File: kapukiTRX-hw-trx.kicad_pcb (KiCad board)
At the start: 4 copper layers, 45.7 x 27.9 mm, 73 parts, among them J1 GPS, J10 Conn_01x01, J11 Conn_01x01, J12 Conn_01x01, J13 Conn_01x01, J14 Conn_01x01, J15 Conn_01x01, J16 Conn_01x01, J17 Conn_01x01, J18 Conn_01x01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

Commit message: Use crystal with smaller footprint
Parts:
- added C33: 100n, Capacitor_SMD:C_0402_1005Metric, F.Cu at (226.1, 99.1)
- added C34: 100n, Capacitor_SMD:C_0402_1005Metric, F.Cu at (223.5, 104.6)
- added C35: 6n8, Capacitor_SMD:C_0402_1005Metric, F.Cu at (229.0, 99.1)
- added C36: 120n, Capacitor_SMD:C_0402_1005Metric, F.Cu at (226.1, 101.0)
- added C37: 100n, Capacitor_SMD:C_0402_1005Metric, F.Cu at (229.0, 101.0)
- added C38: 100n, Capacitor_SMD:C_0402_1005Metric, F.Cu at (226.4, 103.0)
- added C39: 22p, Capacitor_SMD:C_0402_1005Metric, F.Cu at (231.9, 99.1)
- added C40: 22p, Capacitor_SMD:C_0402_1005Metric, F.Cu at (226.4, 105.0)
- added R10: 4k7, Resistor_SMD:R_0402_1005Metric, F.Cu at (231.9, 101.0)
- added R11: 4k7, Resistor_SMD:R_0402_1005Metric, F.Cu at (229.3, 103.0)
- added R12: 10k, Resistor_SMD:R_0402_1005Metric, F.Cu at (229.3, 105.0)
- added R13: 10k, Resistor_SMD:R_0402_1005Metric, F.Cu at (232.2, 103.0)
- added U7: BNO055, Package_LGA:LGA-28_5.2x3.8mm_P0.5mm, F.Cu at (221.1, 100.8)
- added Y2: 32.768kHz, Crystal:Crystal_SMD_2012-2Pin_2.0x1.2mm_HandSoldering, F.Cu at (219.8, 105.0)

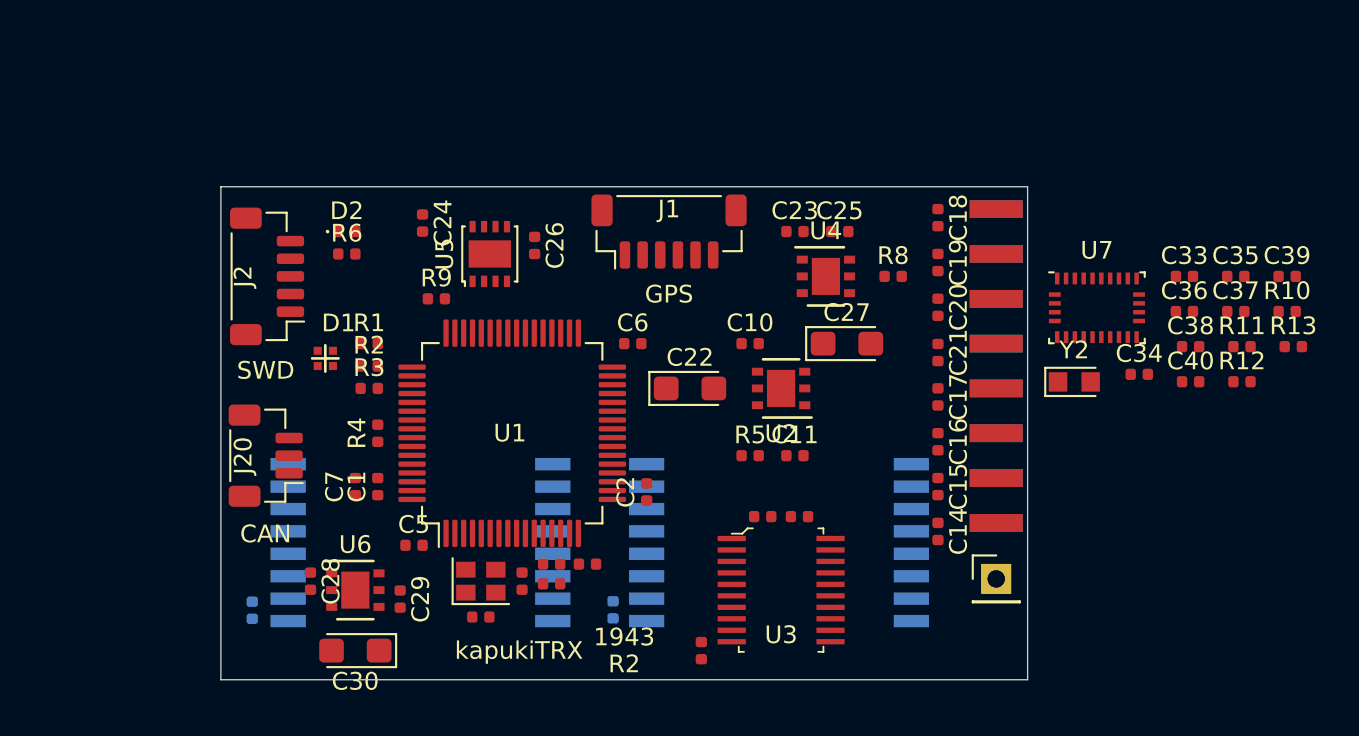
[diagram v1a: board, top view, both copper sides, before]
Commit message: Change processor to G4 series
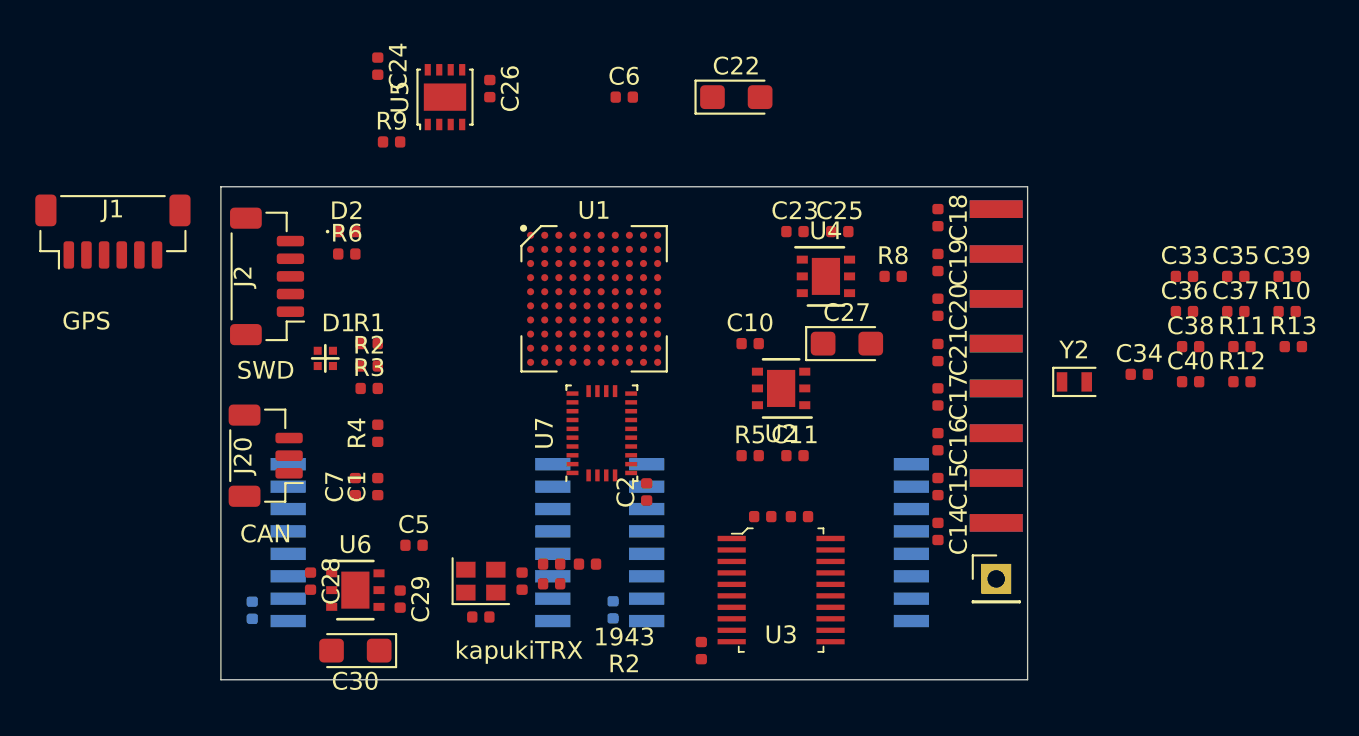
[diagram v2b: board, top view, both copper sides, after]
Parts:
- U1: value STM32L476RGTx -> STM32G474VE; footprint Package_QFP:LQFP-64_10x10mm_P0.5mm -> miscellaneous:TFBGA-100_10x10_8.0x8.0mm
- Y2: footprint Crystal:Crystal_SMD_2012-2Pin_2.0x1.2mm_HandSoldering -> Crystal:Crystal_SMD_2012-2Pin_2.0x1.2mm
- moved J1 31.5 mm to (165.3, 96.5)
- moved U7 28.9 mm to (193.0, 108.0), turned to 90 degrees
- moved C22 16.7 mm to (200.7, 88.9)
- moved C6 14.0 mm to (194.3, 88.9)
- moved C24 9.25 mm to (180.3, 87.1)
- moved C26 9.25 mm to (186.7, 88.4)
- moved R9 9.25 mm to (181.1, 91.4)
- moved U5 9.25 mm to (184.2, 88.9)
- moved U1 8.92 mm to (192.6, 100.3), turned to 0 degrees
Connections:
- R4 pad 2: GND -> Net-(R4-Pad2)
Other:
- net class Default: clearance 0.2 -> 0.127; trace_width 0.25 -> 0.127; via_dia 0.8 -> 0.508; via_drill 0.4 -> 0.254
- rule trace_clearance: 0.2 -> 0.127
- rule trace_min: 0.2 -> 0.127
- rule via_min_drill: 0.3 -> 0.254
- rule via_min_size: 0.4 -> 0.508

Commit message: Placing components and start routing
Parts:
- C1, C2, C35, C36, C6, C7, J10, J12, J14, J16, J18, J4, J6, J8: moved to B.Cu
- J11, J13, J15, J17, J3, J5, J7, J9: moved to F.Cu
- moved J1 43.3 mm to (202.2, 119.3), turned to 180 degrees
- moved C39 42.7 mm to (189.9, 107.1)
- moved R10 41.6 mm to (190.6, 106.2)
- moved R11 38.7 mm to (190.7, 105.0)
- moved C40 37.2 mm to (189.5, 109.2), turned to 270 degrees
- moved C35 36.5 mm to (193.8, 108.7), turned to 270 degrees
- moved R13 35.2 mm to (197.4, 107.6), turned to 270 degrees
- moved R12 34.7 mm to (195.2, 111.6)
- moved C36 32.2 mm to (194.8, 108.7), turned to 270 degrees
- moved C34 31.1 mm to (193.2, 111.6), turned to 180 degrees
- moved R8 29.6 mm to (180.5, 104.8), turned to 90 degrees
- moved Y2 29.1 mm to (191.0, 109.0), turned to 270 degrees
- moved C23 24.3 mm to (180.5, 102.5), turned to 180 degrees
- moved C25 23.9 mm to (185.0, 106.9)
- moved R4 23.7 mm to (196.5, 90.6)
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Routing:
- net IN: track 0.00 -> 106.8 mm, vias 0 -> 5
- net /VCCCPU: track 0.00 -> 88.3 mm, vias 0 -> 9
- net GND: track 0.00 -> 62.4 mm, vias 0 -> 47
- net /Connectors/VCCOUT: track 0.00 -> 37.0 mm, vias 0 -> 2
- net /RF modules/VCCRF: track 0.00 -> 29.4 mm, vias 0 -> 1
- net Net-(C18-Pad1): track 0.00 -> 15.0 mm
- net Net-(C19-Pad1): track 0.00 -> 13.0 mm
- net Net-(C20-Pad1): track 0.00 -> 11.4 mm
- net Net-(C21-Pad1): track 0.00 -> 9.37 mm
- net Net-(C14-Pad1): track 0.00 -> 9.22 mm
- net Net-(C17-Pad1): track 0.00 -> 7.54 mm
- net Net-(C15-Pad1): track 0.00 -> 7.47 mm
- net Net-(C16-Pad1): track 0.00 -> 6.76 mm
- net Net-(C4-Pad1): track 0.00 -> 6.07 mm
- net Net-(J20-Pad1): track 0.00 -> 3.91 mm
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- added copper zone on In1.Cu, net GND
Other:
- net class Default: via_dia 0.508 -> 0.4572
- net class IN added: clearance 0.2032, trace_width 0.381, via_dia 0.6858, via_drill 0.3302
- net class VCC added: clearance 0.1524, trace_width 0.254, via_dia 0.4572, via_drill 0.254
- rule pad_to_mask_clearance: 0.051 -> 0.0508
- rule solder_mask_min_width: 0.25 -> 0.1016
- rule via_min_size: 0.508 -> 0.4572

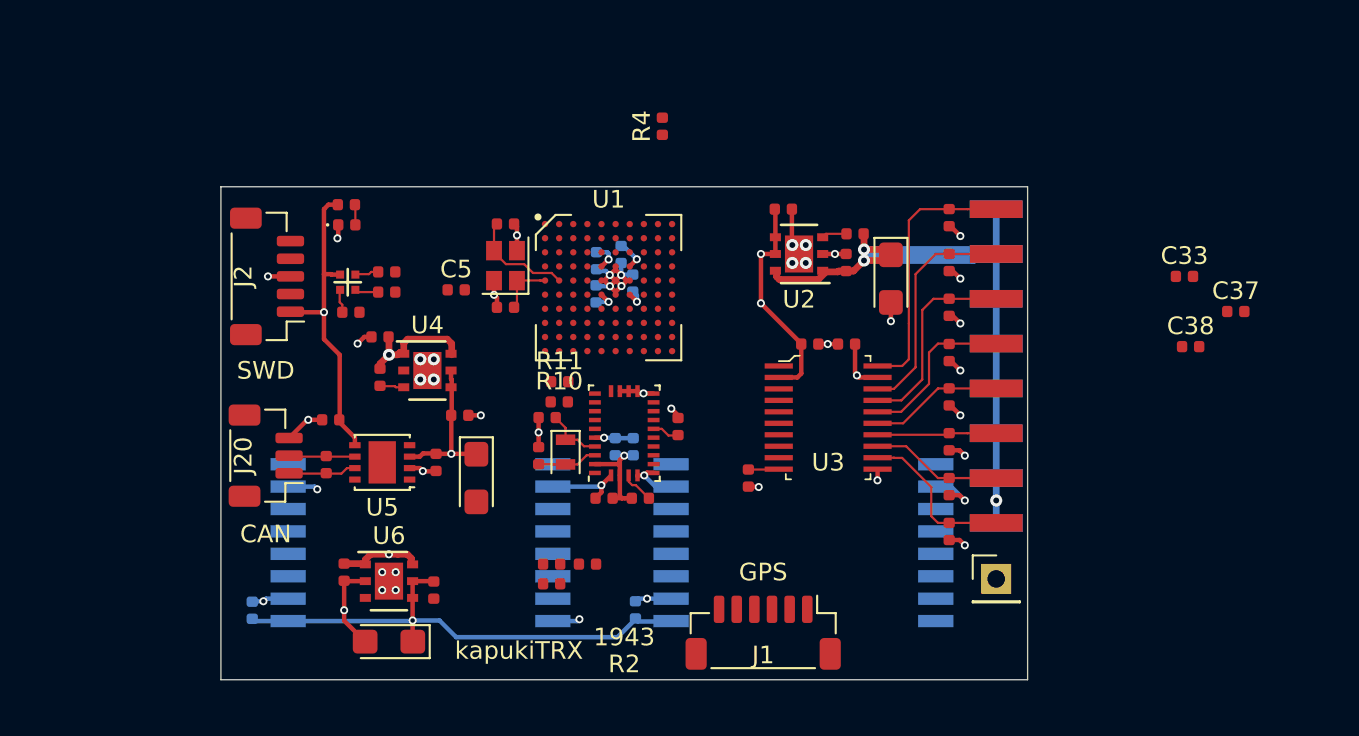
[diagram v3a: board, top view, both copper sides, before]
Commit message: Add nets more nets
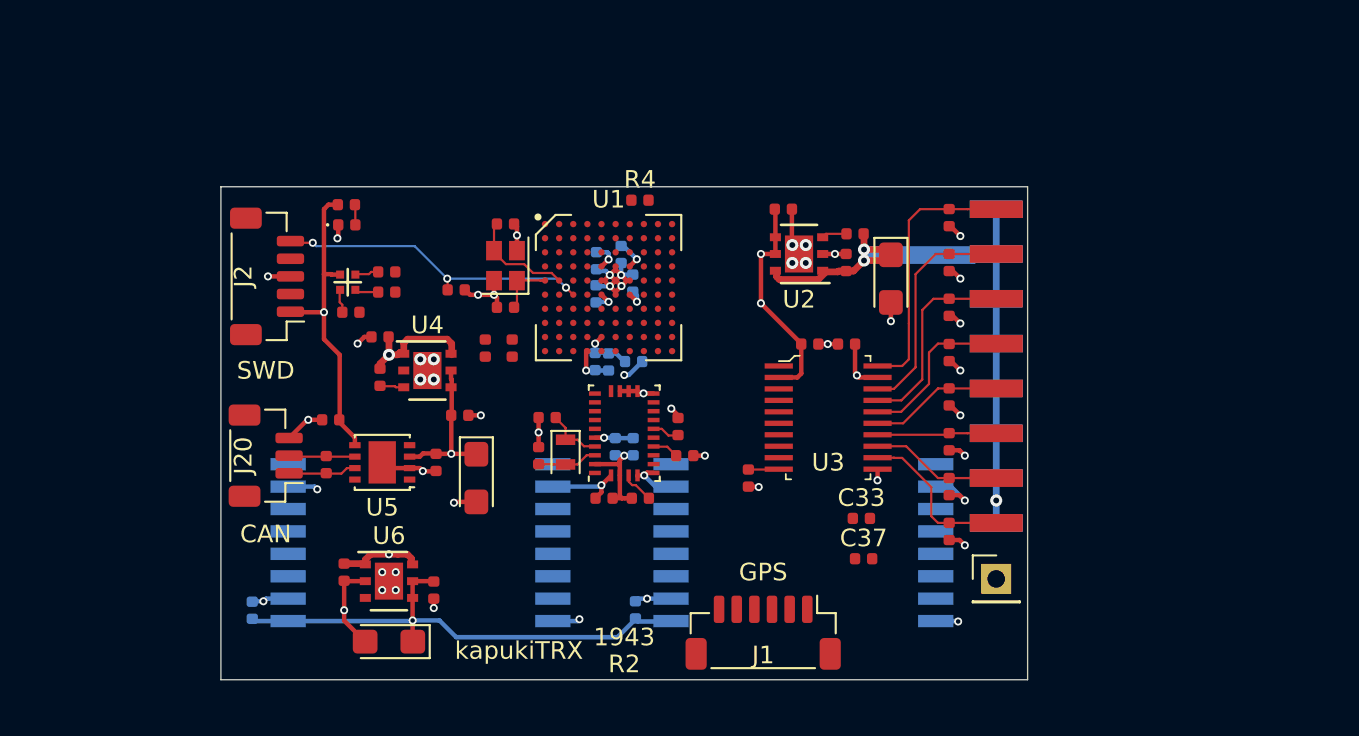
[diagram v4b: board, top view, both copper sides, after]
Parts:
- C8, C9, FB1: moved to B.Cu
- moved C38 29.3 mm to (197.7, 109.2)
- moved C37 25.3 mm to (207.9, 115.1)
- moved C33 22.9 mm to (207.7, 112.8)
- moved C9 13.0 mm to (193.4, 103.9), turned to 270 degrees
- moved FB1 11.8 mm to (194.8, 103.9)
- moved C8 11.7 mm to (192.7, 103.9), turned to 270 degrees
- moved R10 5.18 mm to (186.4, 103.1), turned to 270 degrees
- moved R4 4.38 mm to (195.2, 94.7), turned to 0 degrees
- moved R11 3.30 mm to (188.0, 103.1), turned to 270 degrees
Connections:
- net Net-(U1-PadG8) renamed /BMPINT
- R10 pad 2: /Sensors/SDA -> /SDA
- R11 pad 2: /Sensors/SCL -> /SCL
- R13 pad 2: /Sensors/BNORESET -> /BNORESET
- R4 pad 1: Net-(R4-Pad1) -> /TXMODE
- R4 pad 2: Net-(R4-Pad2) -> GND
- U1 pad A1: Net-(U1-PadA1) -> /LEDGREEN
- U1 pad A10: Net-(U1-PadA10) -> /PWM7
- U1 pad A2: Net-(U1-PadA2) -> /SDA
- U1 pad A3: Net-(U1-PadA3) -> /SCL
- U1 pad A4: Net-(U1-PadA4) -> /RF2MISO
- U1 pad A5: Net-(U1-PadA5) -> /GPSRX
- U1 pad A6: Net-(U1-PadA6) -> /PWM3
- U1 pad A7: Net-(U1-PadA7) -> /TXMODE
- U1 pad A8: Net-(U1-PadA8) -> /PWM2
- U1 pad B1: Net-(U1-PadB1) -> /LEDBLUE
- U1 pad B10: Net-(U1-PadB10) -> /SWCLK
- U1 pad B2: Net-(U1-PadB2) -> /LEDRED
- U1 pad B4: Net-(U1-PadB4) -> /RF2MOSI
- U1 pad B5: Net-(U1-PadB5) -> /RF2CLK
- U1 pad B6: Net-(U1-PadB6) -> /PWM4
- U1 pad B9: Net-(U1-PadB9) -> /PWM1
- U1 pad C2: Net-(U1-PadC2) -> /CANEN
- U1 pad C5: Net-(U1-PadC5) -> /CANTX
- U1 pad D10: Net-(U1-PadD10) -> /GPSTX
- U1 pad D8: Net-(U1-PadD8) -> /SWDIO
- U1 pad D9: Net-(U1-PadD9) -> /CANRX
- U1 pad E10: Net-(U1-PadE10) -> /GPSPPS
- U1 pad E3: Net-(U1-PadE3) -> /PWM8
- U1 pad E9: Net-(U1-PadE9) -> /GPSEN
- U1 pad F10: Net-(U1-PadF10) -> /PWMOE
- U1 pad G1: Net-(U1-PadG1) -> /RF2RXEN
- U1 pad G10: Net-(U1-PadG10) -> /RF1TXEN
- U1 pad G4: Net-(U1-PadG4) -> /PWM5
- U1 pad H1: Net-(U1-PadH1) -> /PWM6
- U1 pad H10: Net-(U1-PadH10) -> /RF1NRESET
- U1 pad H2: Net-(U1-PadH2) -> /RF2NSS
- U1 pad H4: Net-(U1-PadH4) -> /RFPOWEREN
- U1 pad H7: Net-(U1-PadH7) -> /BNORESET
- U1 pad H8: Net-(U1-PadH8) -> /BNOINT
- U1 pad H9: Net-(U1-PadH9) -> /RF1MISO
- U1 pad J10: Net-(U1-PadJ10) -> /RF1BUSY
- U1 pad J3: Net-(U1-PadJ3) -> /RF2NRESET
- U1 pad J9: Net-(U1-PadJ9) -> /RF1CLK
- U1 pad K10: Net-(U1-PadK10) -> /RF1IRQ
- U1 pad K2: Net-(U1-PadK2) -> /RF2BUSY
- U1 pad K3: Net-(U1-PadK3) -> /RF2TXEN
- U1 pad K6: Net-(U1-PadK6) -> /RF2IRQ
- U1 pad K7: Net-(U1-PadK7) -> /RF1RXEN
- U1 pad K8: Net-(U1-PadK8) -> /RF1NSS
- U1 pad K9: Net-(U1-PadK9) -> /RF1MOSI
- U5 pad 8: /Connectors/CANEN -> /CANEN
- U7 pad 11: /Sensors/BNORESET -> /BNORESET
- U7 pad 14: /Sensors/BNOINT -> /BNOINT
- U7 pad 19: /Sensors/SCL -> /SCL
- U7 pad 20: /Sensors/SDA -> /SDA
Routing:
- net /NRST: track 0.00 -> 17.9 mm, vias 0 -> 3
- net GND: track 62.4 -> 71.9 mm, vias 47 -> 53
- net /VCCCPU: track 88.3 -> 92.1 mm, vias 9 -> 10
- net /VDDA: track 0.00 -> 2.88 mm, vias 0 -> 1
- net /Sensors/BNORESET: track 1.54 -> 0.00 mm
- net /BNORESET: track 0.00 -> 1.54 mm
- net Net-(C38-Pad1): track 0.00 -> 1.50 mm
